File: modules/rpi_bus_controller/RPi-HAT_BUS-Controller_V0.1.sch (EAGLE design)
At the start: 52 parts, among them IC1 MC34063AD, IC2 ADUM1201ARZ, IC3 P89LPC922FDH,512FDH, IC4 24LC-I/OT, Q1 ASF1, T1 BC856, T2 BCP52, T3 BC847

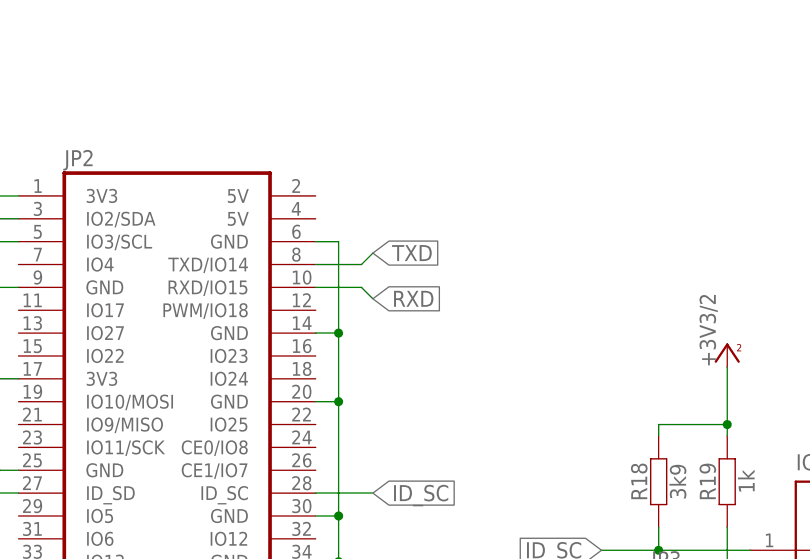
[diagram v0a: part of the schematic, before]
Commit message: TXD RXD getauscht
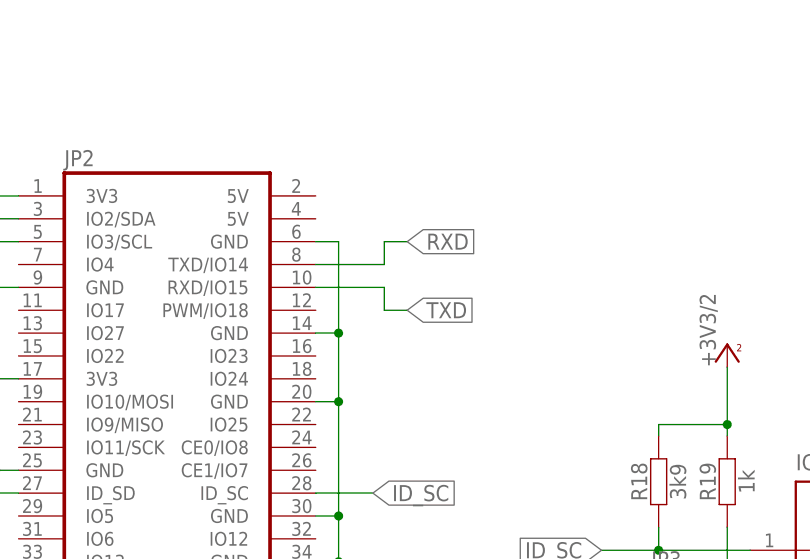
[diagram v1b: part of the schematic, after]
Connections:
- net RXD: now also JP2.TXD/IO14; no longer JP2.RXD/IO15
- net TXD: now also JP2.RXD/IO15; no longer JP2.TXD/IO14
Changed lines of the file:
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@@
 <?xml version="1.0" encoding="utf-8"?>
 <!DOCTYPE eagle SYSTEM "eagle.dtd">
-<eagle version="7.2.0">
+<eagle version="7.4.0">
 <drawing>
 <settings>
@@
 <setting verticaltext="up"/>
 </settings>
-<grid distance="0.1" unitdist="inch" unit="inch" style="lines" multiple="1" display="no" altdistance="0.01" altunitdist="inch" altunit="inch"/>
+<grid distance="0.05" unitdist="inch" unit="inch" style="lines" multiple="1" display="no" altdistance="0.01" altunitdist="inch" altunit="inch"/>
 <layers>
 <layer number="1" name="Top" color="4" fill="1" visible="no" active="no"/>
@@
 <net name="TXD" class="0">
 <segment>
-<pinref part="JP2" gate="G$1" pin="TXD/IO14"/>
-<wire x1="165.1" y1="144.78" x2="170.18" y2="144.78" width="0.1524" layer="91"/>
-<wire x1="170.18" y1="144.78" x2="171.45" y2="146.05" width="0.1524" layer="91"/>
-<label x="171.45" y="146.05" size="1.778" layer="95" xref="yes"/>
-</segment>
-<segment>
 <pinref part="JP1" gate="G$1" pin="4"/>
 <wire x1="314.96" y1="106.68" x2="303.53" y2="106.68" width="0.1524" layer="91"/>
@@
 <wire x1="266.7" y1="63.5" x2="265.43" y2="64.77" width="0.1524" layer="91"/>
 <label x="265.43" y="64.77" size="1.778" layer="95" rot="R180" xref="yes"/>
+<label x="175.26" y="139.7" size="1.778" layer="95" xref="yes"/>
+</segment>
+<segment>
+<pinref part="JP2" gate="G$1" pin="RXD/IO15"/>
+<wire x1="165.1" y1="142.24" x2="172.72" y2="142.24" width="0.1524" layer="91"/>
+<wire x1="172.72" y1="142.24" x2="172.72" y2="139.7" width="0.1524" layer="91"/>
+<wire x1="172.72" y1="139.7" x2="175.26" y2="139.7" width="0.1524" layer="91"/>
 </segment>
 </net>
 <net name="RXD" class="0">
-<segment>
-<pinref part="JP2" gate="G$1" pin="RXD/IO15"/>
-<wire x1="165.1" y1="142.24" x2="170.18" y2="142.24" width="0.1524" layer="91"/>
-<wire x1="170.18" y1="142.24" x2="171.45" y2="140.97" width="0.1524" layer="91"/>
-<label x="171.45" y="140.97" size="1.778" layer="95" xref="yes"/>
-</segment>
 <segment>
 <pinref part="JP1" gate="G$1" pin="5"/>
@@
 <wire x1="267.97" y1="60.96" x2="265.43" y2="60.96" width="0.1524" layer="91"/>
 <label x="265.43" y="60.96" size="1.778" layer="95" rot="R180" xref="yes"/>
-</segment>
-</net>
+<label x="175.26" y="147.32" size="1.778" layer="95" xref="yes"/>
+</segment>
+<segment>
+<pinref part="JP2" gate="G$1" pin="TXD/IO14"/>
+<wire x1="165.1" y1="144.78" x2="172.72" y2="144.78" width="0.1524" layer="91"/>
+<wire x1="172.72" y1="144.78" x2="172.72" y2="147.32" width="0.1524" layer="91"/>
+<wire x1="172.72" y1="147.32" x2="175.26" y2="147.32" width="0.1524" layer="91"/>
+</segment>
+</net>
